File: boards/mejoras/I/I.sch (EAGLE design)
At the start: 5 parts

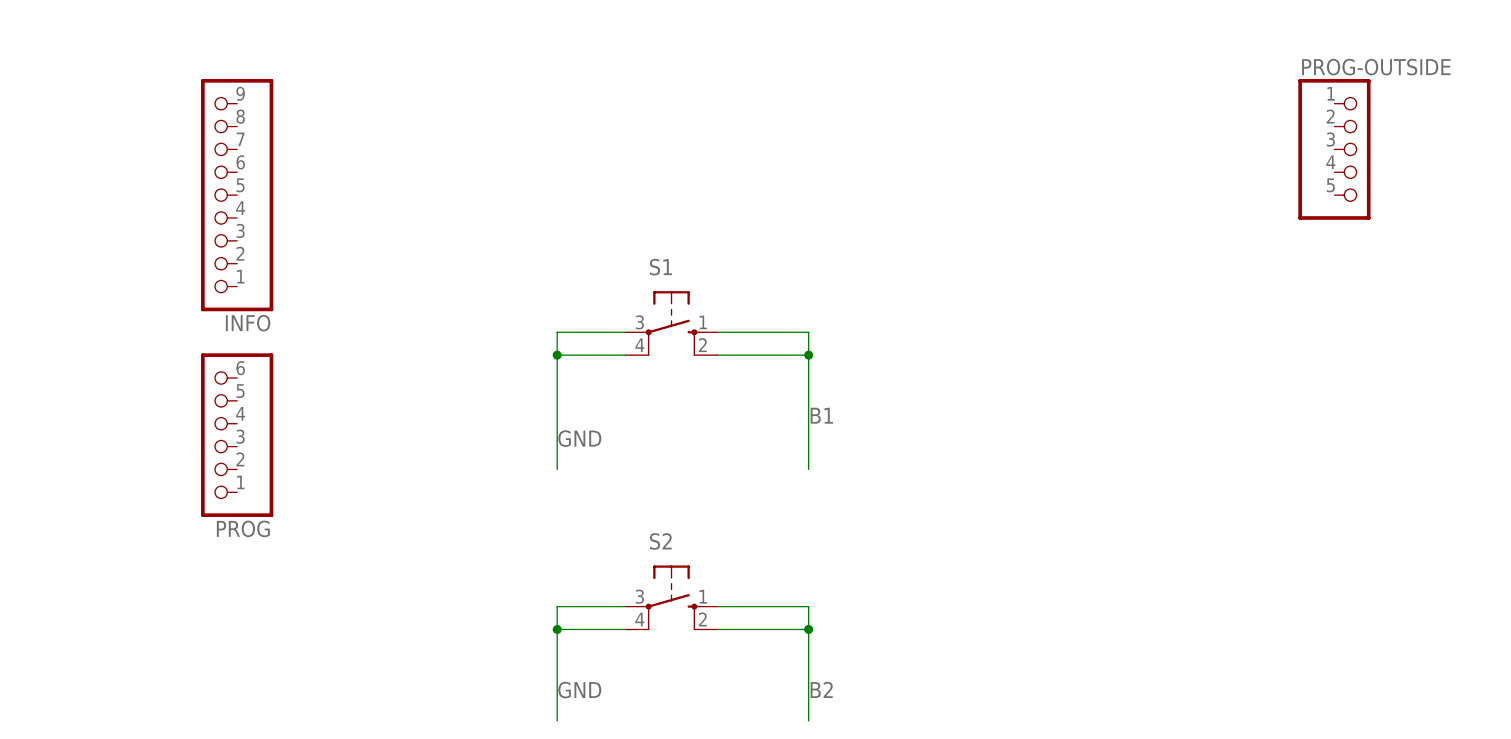
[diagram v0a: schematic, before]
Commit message: added circuit H and I
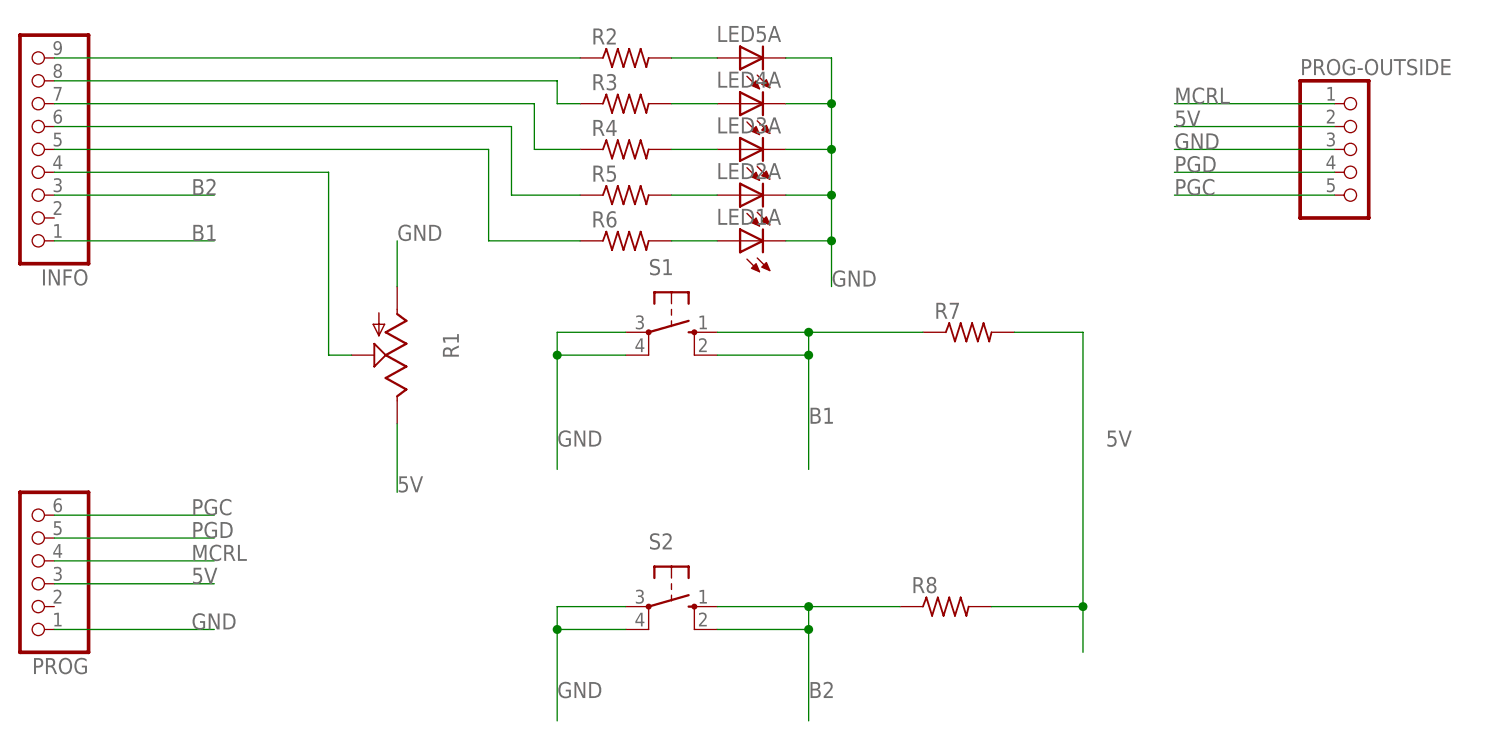
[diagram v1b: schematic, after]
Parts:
- added LED1A, LED2A, LED3A, LED4A, LED5A: (no value), adafruit:LEDCHIPLED_1206
- added R1: (no value), pot:TRIM_US-CA6V
- added R2, R3, R4, R5, R6, R7, R8: (no value), rcl:R-US_M1206
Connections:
- new net 5V: PROG-OUTSIDE.2, PROG.3, R1.E, R7.2, R8.2
- new net MCRL: PROG-OUTSIDE.1, PROG.4
- new net N$1: LED1A.A, R6.2
- new net N$10: INFO.5, R6.1
- new net N$11: INFO.4, R1.S
- new net N$2: LED2A.A, R5.2
- new net N$3: LED3A.A, R4.2
- new net N$4: LED4A.A, R3.2
- new net N$5: LED5A.A, R2.2
- new net N$6: INFO.9, R2.1
- new net N$7: INFO.8, R3.1
- new net N$8: INFO.7, R4.1
- new net N$9: INFO.6, R5.1
- new net PGC: PROG-OUTSIDE.5, PROG.6
- new net PGD: PROG-OUTSIDE.4, PROG.5
- net B1: now also INFO.1, R7.1
- net B2: now also INFO.3, R8.1
- net GND: now also LED1A.C, LED2A.C, LED3A.C, LED4A.C, LED5A.C, PROG-OUTSIDE.3, PROG.1, R1.A
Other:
- moved on the sheet: INFO, PROG

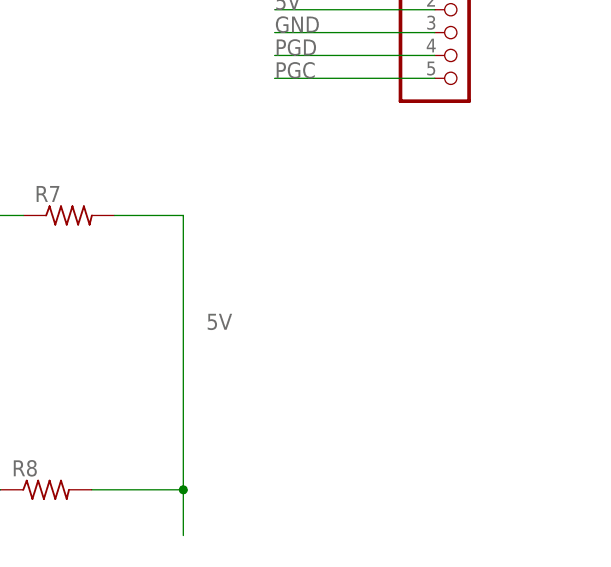
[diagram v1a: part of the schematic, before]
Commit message: added on button
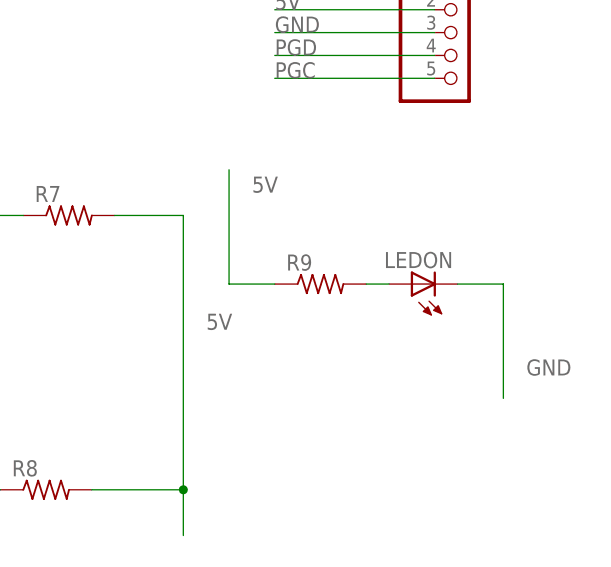
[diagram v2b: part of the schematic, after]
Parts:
- added LEDON: (no value), adafruit:LEDCHIPLED_1206
- added R9: (no value), rcl:R-US_M1206
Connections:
- new net N$12: LEDON.A, R9.2
- net 5V: now also R9.1
- net GND: now also LEDON.C
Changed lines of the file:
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@@
 <part name="R7" library="rcl" library_urn="urn:adsk.eagle:library:334" deviceset="R-US_" device="M1206" package3d_urn="urn:adsk.eagle:package:23566/2"/>
 <part name="R8" library="rcl" library_urn="urn:adsk.eagle:library:334" deviceset="R-US_" device="M1206" package3d_urn="urn:adsk.eagle:package:23566/2"/>
+<part name="LEDON" library="adafruit" library_urn="urn:adsk.eagle:library:420" deviceset="LED" device="CHIPLED_1206" package3d_urn="urn:adsk.eagle:package:6240560/1"/>
+<part name="R9" library="rcl" library_urn="urn:adsk.eagle:library:334" deviceset="R-US_" device="M1206" package3d_urn="urn:adsk.eagle:package:23566/2"/>
 </parts>
 <sheets>
@@
 <attribute name="NAME" x="29.21" y="31.9786" size="1.778" layer="95"/>
 <attribute name="VALUE" x="29.21" y="27.178" size="1.778" layer="96"/>
+</instance>
+<instance part="LEDON" gate="G$1" x="73.66" y="53.34" smashed="yes" rot="R90">
+<attribute name="NAME" x="78.232" y="56.896" size="1.778" layer="95" rot="R180"/>
+<attribute name="VALUE" x="78.232" y="59.055" size="1.778" layer="96" rot="R180"/>
+</instance>
+<instance part="R9" gate="G$1" x="63.5" y="53.34" smashed="yes">
+<attribute name="NAME" x="59.69" y="54.8386" size="1.778" layer="95"/>
+<attribute name="VALUE" x="59.69" y="50.038" size="1.778" layer="96"/>
 </instance>
 </instances>
@@
 <label x="58.42" y="81.28" size="1.778" layer="95"/>
 </segment>
+<segment>
+<pinref part="LEDON" gate="G$1" pin="C"/>
+<wire x1="78.74" y1="53.34" x2="83.82" y2="53.34" width="0.1524" layer="91"/>
+<wire x1="83.82" y1="53.34" x2="83.82" y2="40.64" width="0.1524" layer="91"/>
+<label x="86.36" y="43.18" size="1.778" layer="95"/>
+</segment>
 </net>
 <net name="B1" class="0">
@@
 <label x="58.42" y="83.82" size="1.778" layer="95"/>
 </segment>
+<segment>
+<pinref part="R9" gate="G$1" pin="1"/>
+<wire x1="58.42" y1="53.34" x2="53.34" y2="53.34" width="0.1524" layer="91"/>
+<wire x1="53.34" y1="53.34" x2="53.34" y2="66.04" width="0.1524" layer="91"/>
+<label x="55.88" y="63.5" size="1.778" layer="95"/>
+</segment>
 </net>
 <net name="PGC" class="0">
@@
 </segment>
 </net>
+<net name="N$12" class="0">
+<segment>
+<pinref part="R9" gate="G$1" pin="2"/>
+<pinref part="LEDON" gate="G$1" pin="A"/>
+<wire x1="68.58" y1="53.34" x2="71.12" y2="53.34" width="0.1524" layer="91"/>
+</segment>
+</net>

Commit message: small fixes to g and i
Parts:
- R1: device pot:TRIM_US-CA6V -> pot-enhanced:TRIM_US-CA6V
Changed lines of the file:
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@@
 <grid distance="0.1" unitdist="inch" unit="inch" style="lines" multiple="1" display="no" altdistance="0.01" altunitdist="inch" altunit="inch"/>
 <layers>
-<layer number="1" name="Top" color="4" fill="1" visible="no" active="no"/>
-<layer number="16" name="Bottom" color="1" fill="1" visible="no" active="no"/>
-<layer number="17" name="Pads" color="2" fill="1" visible="no" active="no"/>
-<layer number="18" name="Vias" color="2" fill="1" visible="no" active="no"/>
-<layer number="19" name="Unrouted" color="6" fill="1" visible="no" active="no"/>
-<layer number="20" name="Dimension" color="15" fill="1" visible="no" active="no"/>
-<layer number="21" name="tPlace" color="7" fill="1" visible="no" active="no"/>
-<layer number="22" name="bPlace" color="7" fill="1" visible="no" active="no"/>
-<layer number="23" name="tOrigins" color="15" fill="1" visible="no" active="no"/>
-<layer number="24" name="bOrigins" color="15" fill="1" visible="no" active="no"/>
-<layer number="25" name="tNames" color="7" fill="1" visible="no" active="no"/>
-<layer number="26" name="bNames" color="7" fill="1" visible="no" active="no"/>
-<layer number="27" name="tValues" color="7" fill="1" visible="no" active="no"/>
-<layer number="28" name="bValues" color="7" fill="1" visible="no" active="no"/>
+<layer number="1" name="Top" color="4" fill="1" visible="yes" active="no"/>
+<layer number="16" name="Bottom" color="1" fill="1" visible="yes" active="no"/>
+<layer number="17" name="Pads" color="2" fill="1" visible="yes" active="no"/>
+<layer number="18" name="Vias" color="2" fill="1" visible="yes" active="no"/>
+<layer number="19" name="Unrouted" color="6" fill="1" visible="yes" active="no"/>
+<layer number="20" name="Dimension" color="24" fill="1" visible="yes" active="no"/>
+<layer number="21" name="tPlace" color="7" fill="1" visible="yes" active="no"/>
+<layer number="22" name="bPlace" color="7" fill="1" visible="yes" active="no"/>
+<layer number="23" name="tOrigins" color="15" fill="1" visible="yes" active="no"/>
+<layer number="24" name="bOrigins" color="15" fill="1" visible="yes" active="no"/>
+<layer number="25" name="tNames" color="7" fill="1" visible="yes" active="no"/>
+<layer number="26" name="bNames" color="7" fill="1" visible="yes" active="no"/>
+<layer number="27" name="tValues" color="7" fill="1" visible="yes" active="no"/>
+<layer number="28" name="bValues" color="7" fill="1" visible="yes" active="no"/>
 <layer number="29" name="tStop" color="7" fill="3" visible="no" active="no"/>
 <layer number="30" name="bStop" color="7" fill="6" visible="no" active="no"/>
@@
 <layer number="35" name="tGlue" color="7" fill="4" visible="no" active="no"/>
 <layer number="36" name="bGlue" color="7" fill="5" visible="no" active="no"/>
-<layer number="37" name="tTest" color="7" fill="1" visible="no" active="no"/>
-<layer number="38" name="bTest" color="7" fill="1" visible="no" active="no"/>
+<layer number="37" name="tTest" color="7" fill="1" visible="yes" active="no"/>
+<layer number="38" name="bTest" color="7" fill="1" visible="yes" active="no"/>
 <layer number="39" name="tKeepout" color="4" fill="11" visible="no" active="no"/>
 <layer number="40" name="bKeepout" color="1" fill="11" visible="no" active="no"/>
@@
 <layer number="44" name="Drills" color="7" fill="1" visible="no" active="no"/>
 <layer number="45" name="Holes" color="7" fill="1" visible="no" active="no"/>
-<layer number="46" name="Milling" color="3" fill="1" visible="no" active="no"/>
-<layer number="47" name="Measures" color="7" fill="1" visible="no" active="no"/>
-<layer number="48" name="Document" color="7" fill="1" visible="no" active="no"/>
-<layer number="49" name="Reference" color="7" fill="1" visible="no" active="no"/>
-<layer number="51" name="tDocu" color="7" fill="1" visible="no" active="no"/>
-<layer number="52" name="bDocu" color="7" fill="1" visible="no" active="no"/>
+<layer number="46" name="Milling" color="3" fill="1" visible="yes" active="no"/>
+<layer number="47" name="Measures" color="7" fill="1" visible="yes" active="no"/>
+<layer number="48" name="Document" color="7" fill="1" visible="yes" active="no"/>
+<layer number="49" name="Reference" color="7" fill="1" visible="yes" active="no"/>
+<layer number="51" name="tDocu" color="7" fill="1" visible="yes" active="no"/>
+<layer number="52" name="bDocu" color="7" fill="1" visible="yes" active="no"/>
 <layer number="88" name="SimResults" color="9" fill="1" visible="yes" active="yes"/>
 <layer number="89" name="SimProbes" color="9" fill="1" visible="yes" active="yes"/>
@@
 <part name="LED2A" library="adafruit" library_urn="urn:adsk.eagle:library:420" deviceset="LED" device="CHIPLED_1206" package3d_urn="urn:adsk.eagle:package:6240560/1"/>
 <part name="LED1A" library="adafruit" library_urn="urn:adsk.eagle:library:420" deviceset="LED" device="CHIPLED_1206" package3d_urn="urn:adsk.eagle:package:6240560/1"/>
-<part name="R1" library="pot" library_urn="urn:adsk.eagle:library:331" deviceset="TRIM_US-" device="CA6V" package3d_urn="urn:adsk.eagle:package:22691/1"/>
+<part name="R1" library="pot-enhanced" deviceset="TRIM_US-" device="CA6V" package3d_urn="urn:adsk.eagle:package:22691/1"/>
 <part name="R2" library="rcl" library_urn="urn:adsk.eagle:library:334" deviceset="R-US_" device="M1206" package3d_urn="urn:adsk.eagle:package:23566/2"/>
 <part name="R3" library="rcl" library_urn="urn:adsk.eagle:library:334" deviceset="R-US_" device="M1206" package3d_urn="urn:adsk.eagle:package:23566/2"/>
